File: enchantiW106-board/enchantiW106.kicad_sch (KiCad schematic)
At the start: 71 parts, among them J1 USB_C_Receptacle_USB2.0, SW1 B3U-1000P, SW2 B3U-1000P, U1 USBLC6-2P6, U11 MAX17262REWL+T, U12 BQ25185DLHR, U13 ICM-42670-P, U2 MMC5633NJL, U3 IRIS-W106-00B, U4 NCP167AMX330TBG, U5 CP2102N-Axx-xQFN20, U6 ESP-PSRAM64, U7 STM32H562RIVx, U9 NCP167AMX330TBG

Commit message: Fixed mistakes with revision 1 of the board, removed traces from inner layers
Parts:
- removed ANG2: CONN HEADER SMD 2POS 1MM, ENCHANTI_connectors:Molex_Pico-Clasp_2pin_Vertical, symbol ENCHANTI_connectors:PicoClasp_2pin
- removed FP1: CONN HEADER SMD 6POS 1MM, ENCHANTI_connectors:Molex_Pico-Clasp_501331-0607_1x06-1MP_P1.00mm_Vertical, symbol Connector_Generic_MountingPin:Conn_01x06_MountingPin
- removed U6: ESP-PSRAM64, Package_SO:SOIC-8_3.9x4.9mm_P1.27mm, symbol Memory_RAM:ESP-PSRAM32
- removed U7: STM32H562RIVx, Package_DFN_QFN:QFN-68-1EP_8x8mm_P0.4mm_EP6.4x6.4mm, symbol MCU_ST_STM32H5:STM32H562RIVx
- added FP2: CONN HEADER SMD 6POS 1MM, Connector_Molex:Molex_Pico-Clasp_501331-0807_1x08-1MP_P1.00mm_Vertical, symbol ENCHANTI_connectors:PicoClasp_8pin
- added R17: 10k, Resistor_SMD:R_0402_1005Metric, symbol Device:R_US
- added R18: 1k, Resistor_SMD:R_0402_1005Metric, symbol Device:R_US
- R1, R2: value 10k -> 1k; Mfg Part # ERJ-2RKF1002X -> ERJ-2RKF1001X
- R15: value 0.3k -> 0.43k; Mfg Part # ERJ-2RKF3000X -> ERJ-2RKF4300X; mpn ERJ-2RKF2201X -> (none)
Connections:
- net RCE is gone; now on net LED2: U3.A5 (QSPI_RCE)
- net RCLK is gone; now on net LED1: U3.A2 (QSPI_RCLK)
- net +3V3: now also CHARGLED1.2 (A); no longer BOARDLAYOUT1.2.1 (3v3), R12.2, R13.2, R14.2, R16.2
- net 3V3_AUX: now also BOARDLAYOUT1.2.1 (3v3), R12.2, R13.2
- net BLUELED: now also U3.L4 (RMII_INT); no longer U3.M5 (GPIO[48])
- net BTN: now also U3.F3 (RMII_CLK), FP2.3 (Pin_3); no longer U3.N6 (GPIO[47])
- net EN: no longer U5.9 (~{RST})
- net FSR1: now also R1.2; no longer R1.1
- net FSR2: now also R2.2; no longer R2.1
- net GND: now also R1.1, R2.1, FP2.2 (Pin_2), FP2.MP (MountPin); no longer R1.2, R2.2
- net IMU_INT: now also U3.N11 (GPIO[1]); no longer U3.N2 (GPIO[54])
- net LDO_EN: now also U3.M4 (GPIO[50]); no longer U3.E2 (GPIO[27])
- net LED1: now also FP2.5 (Pin_5); no longer U3.M4 (GPIO[50])
- net LED2: now also FP2.6 (Pin_6); no longer U3.N4 (GPIO[51])
- net ORANGELED: now also U3.E2 (GPIO[27]); no longer U3.N5 (GPIO[49])
- net STAT1: now also FP2.8 (Pin_8)
- net STAT2: now also FP2.7 (Pin_7)
- net SYS: now also R17.2; no longer U4.3 (EN)
- net VUSB: now also FP2.1 (Pin_1); no longer CHARGLED1.2 (A)
- net VDD: now reaches C1.1, U5.6 (VDD)
- net VDD: now also R14.2, R16.2, R18.1
- net BTN_FP renamed IO29
- net LED3: no longer names the net of U3.K3 (GPIO[61])
- net LED4: no longer names the net of U3.M3 (GPIO[52])
- net RD0: no longer names the net of U3.B4 (QSPI_RD0)
- net RD1: no longer names the net of U3.A4 (QSPI_RD1)
- net RD2: no longer names the net of U3.B3 (QSPI_RD2)
- net RD3: no longer names the net of U3.A3 (QSPI_RD3)
- new net MAIN_LDO_EN: FP2.4 (Pin_4), R17.1, U4.3 (EN)
- new net RST: R18.2, U5.9 (~{RST})
- no-connect marks 59 -> 70
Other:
- note removed: "BUTTON/ANALOG CONNECTOR"
- note removed: "Comms - SDA: IO21 - SCL: IO14 - USBD+: IO20 - USBD-: IO19 - COPI: 10 - CIPO: 13 - SCLK: 12 - CS0: 11 Peripherals - FSR: IO8 - Button: IO9 - UART TX: IO43 - UART RX: IO44 - Status LED (orange): IO16 - Status LED (blue) I015 Interrupts - IMU Interrupt: IO48 - Touch Interrupt 1: IO4 - Touch Interrupt 2: IO5 - Touch Interrupt 3: IO6 - Touch Interrupt 4: IO7"
- note removed: "PSRAM"
- note removed: "Pinout"
- moved on the sheet: C1, C3, R3, R4, R9, TOUCH1, U2, U4

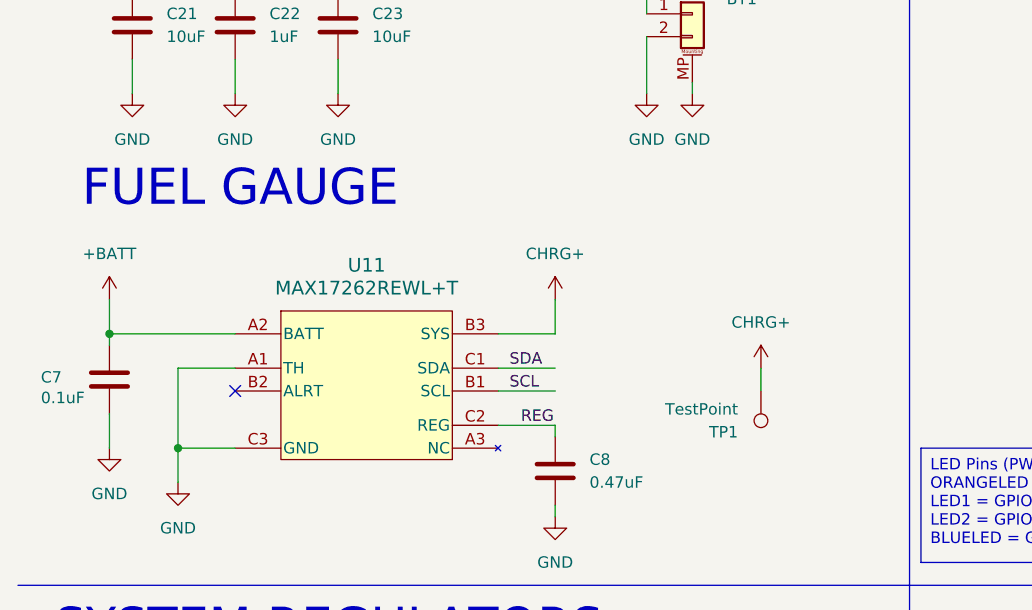
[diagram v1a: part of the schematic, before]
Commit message: change board designto 2 layer board, fix wrong connection for fuel gauge
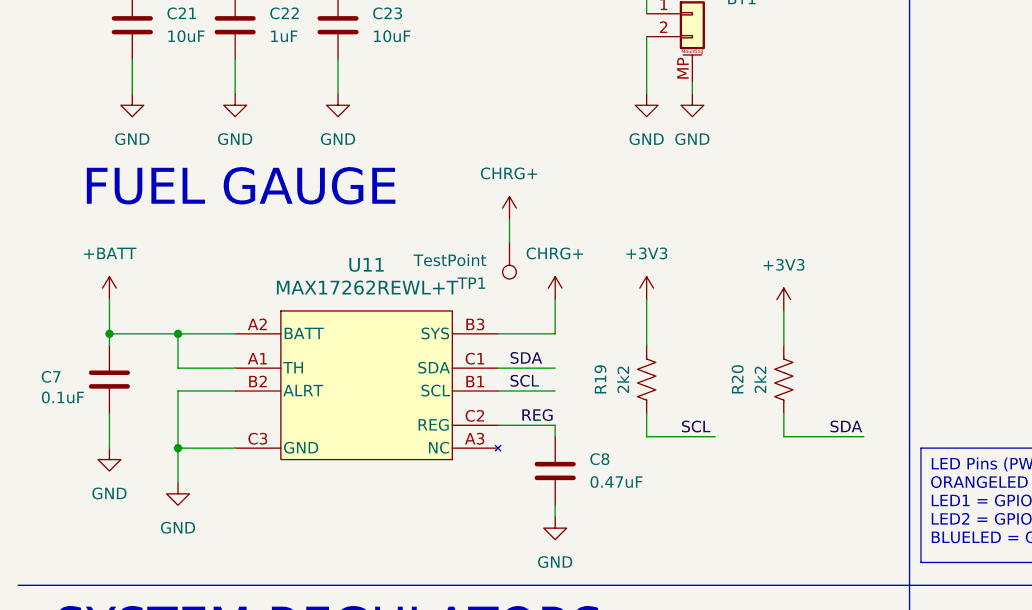
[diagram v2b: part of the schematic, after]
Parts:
- added R19, R20: 2k2, Resistor_SMD:R_0402_1005Metric, symbol Device:R_US
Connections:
- net +3V3: now also R19.2, R20.2
- net +BATT: now also U11.A1 (TH)
- net GND: now also U11.B2 (ALRT); no longer U11.A1 (TH)
- net SCL: now also R19.1
- net SDA: now also R20.1
- no-connect marks 70 -> 69
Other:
- moved on the sheet: TP1

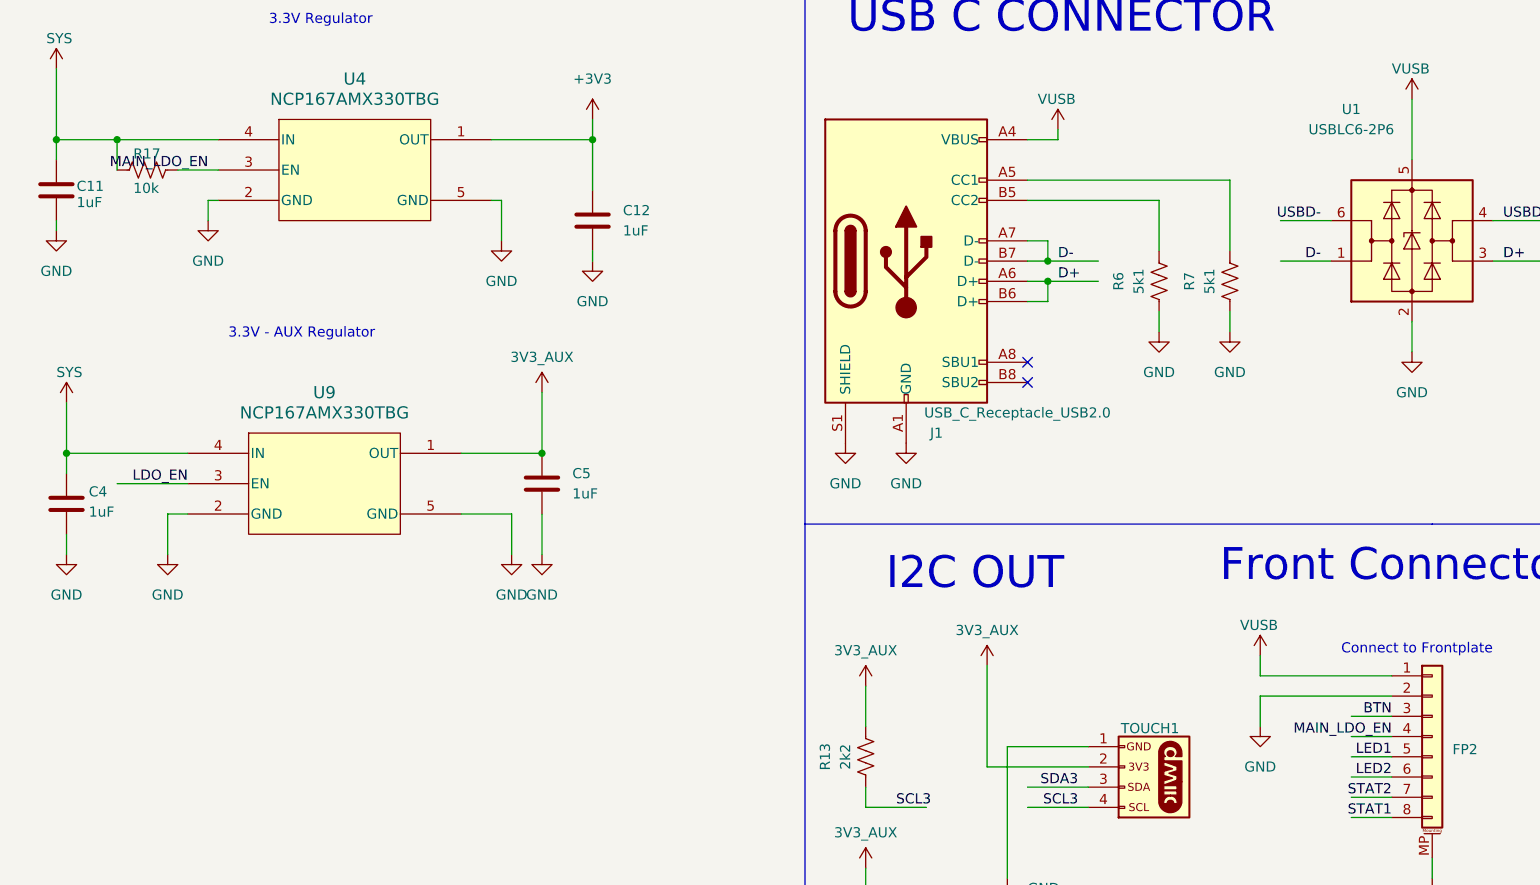
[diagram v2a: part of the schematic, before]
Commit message: updated manufacturing files for enchantiW106, removed unused board files
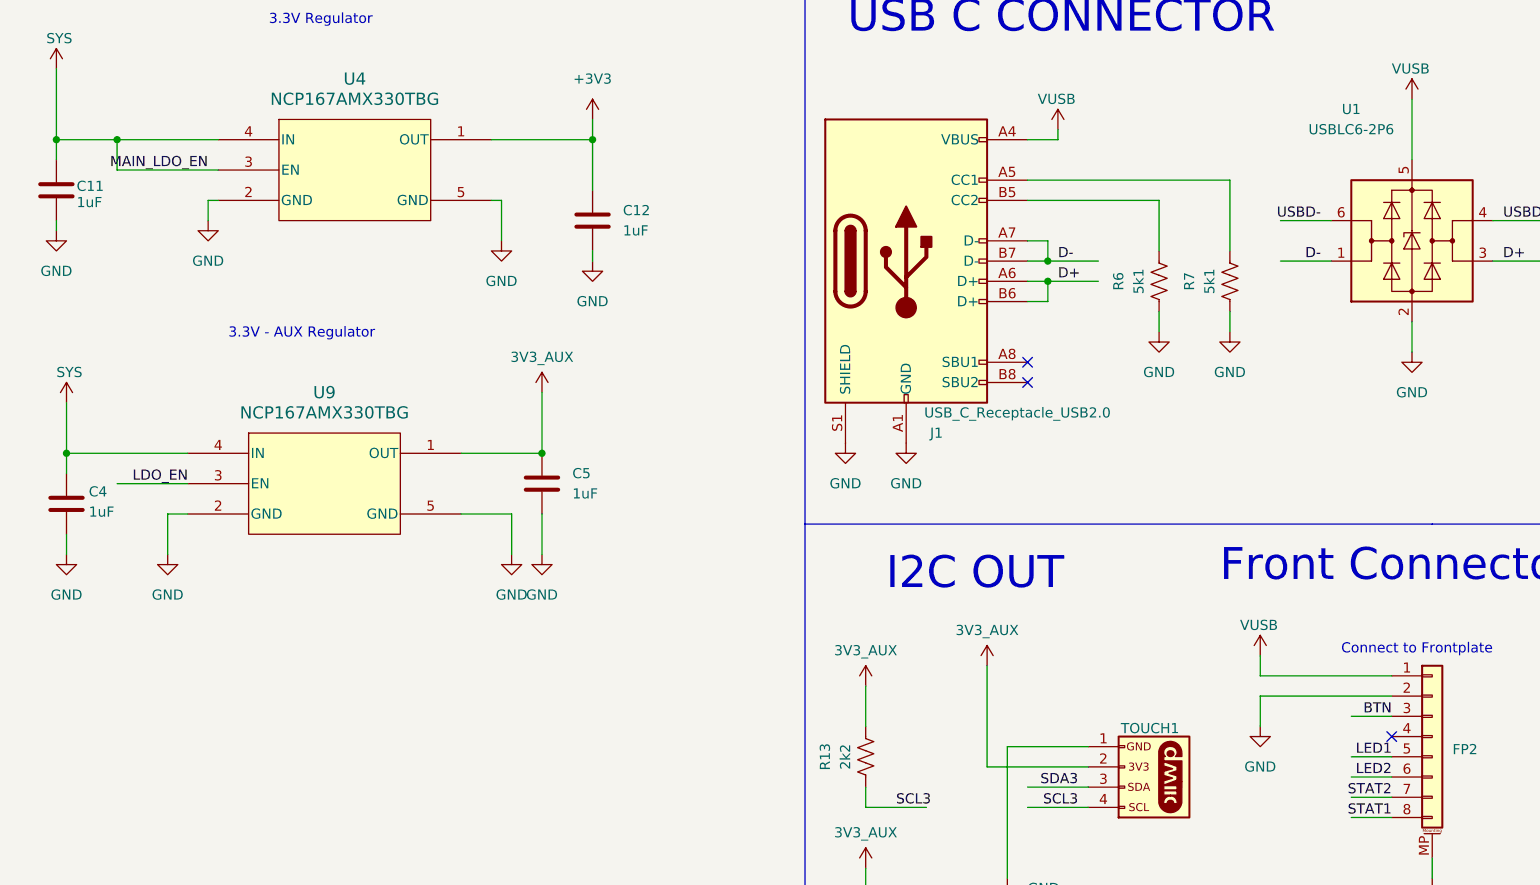
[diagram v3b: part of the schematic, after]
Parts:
- removed R17: 10k, Resistor_SMD:R_0402_1005Metric, symbol Device:R_US
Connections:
- net SYS: now also U4.3 (EN)
- net MAIN_LDO_EN: no longer names the net of FP2.4 (Pin_4)
- net MAIN_LDO_EN: no longer U4.3 (EN)
- no-connect marks 69 -> 70
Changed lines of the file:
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@@
 	)
 	(no_connect
+		(at 184.15 250.19)
+	)
+	(no_connect
 		(at 187.96 71.12)
 	)
@@
 	(wire
 		(pts
-			(xy 179.07 250.19) (xy 184.15 250.19)
-		)
-		(stroke
-			(width 0)
-			(type default)
-		)
-	)
-	(wire
-		(pts
 			(xy 140.97 187.96) (xy 140.97 190.5)
 		)
@@
 	(wire
 		(pts
+			(xy 24.13 179.07) (xy 36.83 179.07)
+		)
+		(stroke
+			(width 0)
+			(type default)
+		)
+	)
+	(wire
+		(pts
 			(xy 48.26 33.02) (xy 43.18 33.02)
 		)
@@
 	(wire
 		(pts
-			(xy 31.75 179.07) (xy 36.83 179.07)
-		)
-		(stroke
-			(width 0)
-			(type default)
-		)
-	)
-	(wire
-		(pts
 			(xy 187.96 111.76) (xy 195.58 111.76)
 		)
@@
 		)
 	)
-	(label "MAIN_LDO_EN"
-		(at 184.15 250.19 180)
-		(fields_autoplaced yes)
-		(effects
-			(font
-				(size 1.27 1.27)
-			)
-			(justify right bottom)
-		)
-	)
 	(label "COPI"
 		(at 361.95 48.26 0)
@@
 					(unit 1)
 				)
-			)
-		)
-	)
-	(symbol
-		(lib_id "Device:R_US")
-		(at 27.94 179.07 270)
-		(unit 1)
-		(exclude_from_sim no)
-		(in_bom yes)
-		(on_board yes)
-		(dnp no)
-		(property "Reference" "R17"
-			(at 26.162 177.038 90)
-			(effects
-				(font
-					(size 1.27 1.27)
-				)
-				(justify left)
-			)
-		)
-		(property "Value" "10k"
-			(at 26.162 181.356 90)
-			(effects
-				(font
-					(size 1.27 1.27)
-				)
-				(justify left)
-			)
-		)
-		(property "Footprint" "Resistor_SMD:R_0402_1005Metric"
-			(at 27.686 180.086 90)
-			(effects
-				(font
-					(size 1.27 1.27)
-				)
-				(hide yes)
-			)
-		)
-		(property "Datasheet" "https://industrial.panasonic.com/cdbs/www-data/pdf/RDA0000/AOA0000C304.pdf"
-			(at 27.94 179.07 0)
-			(effects
-				(font
-					(size 1.27 1.27)
-				)
-				(hide yes)
-			)
-		)
-		(property "Description" "10 kOhms ±1% 0.1W, 1/10W Chip Resistor 0402 (1005 Metric) Automotive AEC-Q200 Thick Film"
-			(at 27.94 179.07 0)
-			(effects
-				(font
-					(size 1.27 1.27)
-				)
-				(hide yes)
-			)
-		)
-		(property "Description Value Pkg" ""
-			(at 27.94 179.07 0)
-			(effects
-				(font
-					(size 1.27 1.27)
-				)
-				(hide yes)
-			)
-		)
-		(property "Mfg Part #" "ERJ-2RKF1002X"
-			(at 27.94 179.07 0)
-			(effects
-				(font
-					(size 1.27 1.27)
-				)
-				(hide yes)
-			)
-		)
-		(property "Manufacturer" "Panasonic Electronic Components"
-			(at 27.94 179.07 0)
-			(effects
-				(font
-					(size 1.27 1.27)
-				)
-				(hide yes)
-			)
-		)
-		(property "mpn" "ERJ-2RKF1001X"
-			(at 27.94 179.07 0)
-			(effects
-				(font
-					(size 1.27 1.27)
-				)
-				(hide yes)
-			)
-		)
-		(pin "1"
-		)
-		(pin "2"
-		)
-		(instances
-			(project "enchantiW106"
-				(path "/1e57a4ff-0c95-4e2b-9e56-d9bf8e99c9a1"
-					(reference "R17")
-					(unit 1)
-				)

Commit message: added version of the board with stm32H5 for sensor processing
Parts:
- removed R14, R16, R18: 1k, Resistor_SMD:R_0402_1005Metric, symbol Device:R_US
- removed R19, R20: 2k2, Resistor_SMD:R_0402_1005Metric, symbol Device:R_US
- removed STATLED3: TX_STAT, LED_SMD:LED_0402_1005Metric, symbol Device:LED
- removed STATLED4: RX_STAT, LED_SMD:LED_0402_1005Metric, symbol Device:LED
- removed U5: CP2102N-Axx-xQFN20, Package_DFN_QFN:SiliconLabs_QFN-20-1EP_3x3mm_P0.5mm_EP1.8x1.8mm, symbol Interface_USB:CP2102N-Axx-xQFN20
- added C10: 4.7uF, Capacitor_SMD:C_0402_1005Metric, symbol Device:C
- added C14: 2.2uF, Capacitor_SMD:C_0402_1005Metric, symbol Device:C
- added C16, C20, C24, C25, C26: 0.1uF, Capacitor_SMD:C_0402_1005Metric, symbol Device:C
- added H4: MountingHole, MountingHole:MountingHole_2.2mm_M2, symbol Mechanical:MountingHole
- added J3: Programming Header, ENCHANTI_connectors:SAMTEC_FTSH-105-01-F-DV-P-TR, symbol ENCHANTI_connectors:Programming_Header
- added U5: STM32H523CET6, ENCHANTI_mcus:LQFP48_STM, symbol ENCHANTI_mcus:STM32H523CET6
- C1, C6: value 0.1uF -> 1uF; Mfg Part # CL05B104KO5NNNC -> CL05A105KO5NNNC; mpn CL05B104KO5NNNC -> CL05A105KO5NNNC
- C2: value 0.1uF -> 2.2uF; Mfg Part # CL05B104KO5NNNC -> CL05A225KP5NSNC; mpn CL05B104KO5NNNC -> (none)
- H1, H2: footprint MountingHole:MountingHole_2.2mm_M2 -> MountingHole:MountingHole_3.2mm_M3
- R4, R9: value 2k2 -> 10k; Mfg Part # ERJ-2RKF2201X -> ERJ-2RKF1002X; mpn ERJ-2RKF2201X -> ERJ-2RKF1002X
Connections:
- net +3V3: now also C6.1, R12.2, R13.2, SW1.2, C10.1, C16.1, C20.1, C24.1, C25.1, C26.1, U5.1 (VBAT), U5.24 (VDD), U5.36 (VDD), U5.48 (VDD), U5.9 (VDDA); no longer ANG1.1 (Pin_1), ANG3.1 (Pin_1), C13.1, C17.1, C18.1, C19.1, C3.1, R5.2, R9.2, U13.5 (VDDIO), U13.8 (VDD), U2.B1 (VDD), U3.H1 (VCC), U3.H2 (VCC), U3.H3 (VCC)
- net 3V3_AUX: now also ANG1.1 (Pin_1), ANG3.1 (Pin_1), C13.1, C17.1, C18.1, C19.1, C3.1, R5.2, U13.5 (VDDIO), U13.8 (VDD), U2.B1 (VDD), U3.H1 (VCC), U3.H2 (VCC), U3.H3 (VCC), J3.1 (VDD); no longer R12.2, R13.2
- net BOOT: no longer SW1.1
- net BTN: now also U5.2 (PC13); no longer U3.F3 (RMII_CLK)
- net EN: now also J3.10 (RES); no longer SW2.1
- net FSR1: now also U5.11 (PA1); no longer U3.M6 (GPIO[46])
- net FSR2: now also U5.12 (PA2); no longer U3.N7 (GPIO[45])
- net GND: now also R9.2, C10.2, C14.2, C16.2, C20.2, C24.2, C25.2, C26.2, J3.3 (GND), J3.5 (GND), J3.9 (GND), U5.23 (VSS), U5.35 (VSS), U5.47 (VSS), U5.8 (VSSA); no longer SW1.2
- net IMU_INT: no longer U3.N11 (GPIO[1])
- net LDO_EN: now also U5.10 (PA0); no longer U3.M4 (GPIO[50])
- net LED2: now also U5.13 (PA3); no longer U3.A5 (QSPI_RCE)
- net USBD+: now also U5.33 (PA12)
- net USBD-: now also U5.32 (PA11)
- net VUSB: no longer C2.1, C6.1
- net CIPO renamed SPI1_CIPO
- net SPI1_CIPO: now also U5.16 (PA6); no longer U3.N10 (GPIO[3])
- net COPI renamed SPI1_COPI
- net SPI1_COPI: now also U5.17 (PA7); no longer U3.M10 (GPIO[2])
- net CS renamed SPI1_CS
- net SPI1_CS: now also U5.14 (PA4); no longer U3.M11 (GPIO[0])
- net CTS: no longer names the net of U3.A9 (SDIO_D1)
- net RTS: no longer names the net of U3.B8 (SDIO_D0)
- net RXD renamed RX
- net SCL: no longer names the net of U3.L2 (RMII_MDC)
- net SCL: no longer U11.B1 (SCL)
- removed net SCL2: R4.1, U2.A2 (SCL), U3.B12 (JTAG_TDI)
- net SCL3 renamed I3C2_SCL
- net I3C2_SCL: now also U5.41 (PB5); no longer R13.1, U3.B5 (FC2_TxD)
- net SCLK renamed SPI1_SCLK
- net SPI1_SCLK: now also U5.15 (PA5); no longer U3.M9 (GPIO[4])
- net SDA: no longer names the net of U3.L1 (RMII_MDIO)
- net SDA: no longer U11.C1 (SDA)
- removed net SDA2: R9.1, U2.B2 (SDA), U3.A12 (JTAG_TDO)
- net SDA3 renamed I3C2_SDA
- net I3C2_SDA: now also U5.40 (PB4); no longer R12.1, U3.A6 (FC2_RxD)
- net TXD renamed TX
- net VDD renamed NRST
- net NRST: now also R4.1, SW2.1, U5.7 (NRST)
- new net: C2.1, U5.46 (VCAP)
- new net: C14.1, U5.22 (VCAP)
- new net BOOT0: R9.1, SW1.1, U5.44 (BOOT0)
- new net I2C2_SCL: R13.1, U11.B1 (SCL), U5.21 (PB10)
- new net I2C2_SDA: R12.1, U11.C1 (SDA), U5.39 (PB3)
- new net I3C1_SCL: U2.A2 (SCL), U5.45 (PB8)
- new net I3C1_SDA: U2.B2 (SDA), U5.43 (PB7)
- new net SPI2_CIPO: U3.N10 (GPIO[3]), U5.27 (PB14)
- new net SPI2_COPI: U3.M10 (GPIO[2]), U5.28 (PB15)
- new net SPI2_CS: U3.M11 (GPIO[0]), U5.25 (PB12)
- new net SPI2_SCLK: U3.M9 (GPIO[4]), U5.26 (PB13)
- new net SWDCLK: J3.4 (SWCLK), U3.A6 (FC2_RxD)
- new net SWDIO: J3.2 (SWDIO), U3.B5 (FC2_TxD)
- no-connect marks 70 -> 93
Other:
- note added: "BUTTONS"
- note added: "STM32H523CE - Sensor Processing Companion"
- note added: "VDD Filtering"
- note added: "VDDA Filtering"
- note removed: "BOOT BUTTON"
- note removed: "MOUNTING HOLES (M3)"
- note removed: "RESET BUTTON"
- moved on the sheet: C11, C12, C15, C17, C18, C3, C4, C5, FP2, H1, H2, H3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
